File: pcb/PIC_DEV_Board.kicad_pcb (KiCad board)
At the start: 2 copper layers, 25.5 x 47.5 mm, 8 parts, among them J1 Conn_01x08_Pin, J3 Conn_01x15_Pin, J4 Conn_01x02_Pin

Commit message: trace updates
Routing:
- net Net-(J3-Pin_11): track 27.6 -> 26.6 mm
- net Net-(J3-Pin_9): track 21.9 -> 21.3 mm
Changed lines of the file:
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@@
 		(tags "resistor")
 		(property "Reference" "R1"
-			(at 0 -1.65 360)
+			(at 0 -1.65 0)
 			(layer "F.SilkS")
 			(effects
@@
 		)
 		(property "Value" "10K"
-			(at 0 1.65 360)
+			(at 0 1.65 0)
 			(layer "F.Fab")
 			(effects
@@
 		)
 		(fp_text user "${REFERENCE}"
-			(at 0 0 360)
+			(at 0 0 0)
 			(layer "F.Fab")
 			(effects
@@
 	)
 	(segment
-		(start 140.2 113.3)
-		(end 144.6 108.9)
+		(start 137 113.3)
+		(end 142.2 113.3)
 		(width 0.2)
 		(layer "F.Cu")
@@
 	)
 	(segment
-		(start 137 113.3)
-		(end 140.2 113.3)
+		(start 142.2 113.3)
+		(end 144.9 110.6)
 		(width 0.2)
 		(layer "F.Cu")
@@
 	)
 	(segment
-		(start 144.6 108.9)
-		(end 144.6 106.834314)
+		(start 144.9 106.834314)
+		(end 150.924314 100.81)
 		(width 0.2)
 		(layer "F.Cu")
@@
 	)
 	(segment
-		(start 144.6 106.834314)
-		(end 150.624314 100.81)
+		(start 144.9 110.6)
+		(end 144.9 106.834314)
 		(width 0.2)
 		(layer "F.Cu")
@@
 	)
 	(segment
-		(start 150.624314 100.81)
-		(end 152.5 100.81)
-		(width 0.2)
-		(layer "F.Cu")
-		(net 13)
-	)
-	(segment
-		(start 150.65 103.35)
-		(end 152.5 103.35)
+		(start 146.1 117)
+		(end 144.72 118.38)
 		(width 0.2)
 		(layer "F.Cu")
@@
 	)
 	(segment
-		(start 146 118)
-		(end 146 108)
+		(start 151.475001 103.35)
+		(end 146.1 108.725001)
 		(width 0.2)
 		(layer "F.Cu")
@@
 	)
 	(segment
-		(start 137 118.38)
-		(end 145.62 118.38)
+		(start 146.1 108.725001)
+		(end 146.1 117)
 		(width 0.2)
 		(layer "F.Cu")
@@
 	)
 	(segment
-		(start 145.62 118.38)
-		(end 146 118)
+		(start 144.72 118.38)
+		(end 137 118.38)
 		(width 0.2)
 		(layer "F.Cu")
@@
 	)
 	(segment
-		(start 146 108)
-		(end 150.65 103.35)
-		(width 0.2)
-		(layer "F.Cu")
+		(start 152.5 103.35)
+		(end 151.475001 103.35)
+		(width 0.2)
+		(layer "F.Cu")

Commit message: silkscreen
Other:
- board text added: "+"
- board text added: "-"
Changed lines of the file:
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@@
 		(tags "LED")
 		(property "Reference" "D1"
-			(at 0.0625 1.5 180)
+			(at -0.1375 -1.9 180)
 			(layer "F.SilkS")
 			(effects
@@
 		(tags "resistor")
 		(property "Reference" "R2"
-			(at -1.475 -2 0)
+			(at 0.0875 1.9 0)
 			(layer "F.SilkS")
 			(effects
@@
 		(tags "Through hole pin header THT 1x02 2.54mm single row")
 		(property "Reference" "J4"
-			(at 0 -2.33 0)
-			(layer "F.SilkS")
+			(at 2.3 -1.3 0)
+			(layer "F.SilkS")
+			(hide yes)
 			(effects
 				(font
@@
 			(at 0 -2.33 0)
 			(layer "F.SilkS")
+			(hide yes)
 			(effects
 				(font
@@
 		(tags "SOIC SO")
 		(property "Reference" "U1"
-			(at 0.15 7.175 0)
+			(at -0.05 7.685 0)
 			(layer "F.SilkS")
 			(effects
@@
 		(layer "Edge.Cuts")
 	)
+	(gr_text "-\n"
+		(at 139.9 86.6 90)
+		(layer "F.SilkS")
+		(effects
+			(font
+				(size 1.5 1.5)
+				(thickness 0.3)
+				(bold yes)
+			)
+			(justify left bottom)
+		)
+	)
+	(gr_text "+"
+		(at 138.1 91.7 0)
+		(layer "F.SilkS")
+		(effects
+			(font
+				(size 1.5 1.5)
+				(thickness 0.3)
+				(bold yes)
+			)
+			(justify left bottom)
+		)
+	)
 	(segment

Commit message: higher functionality board
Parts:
- removed J3: Conn_01x15_Pin, Connector_PinHeader_2.54mm:PinHeader_1x15_P2.54mm_Vertical
- added C2: 30pF, Capacitor_SMD:C_0805_2012Metric, F.Cu at (136.1, 91.9)
- added C3: 30pF, Capacitor_SMD:C_0805_2012Metric, F.Cu at (136.1, 95.0)
- added C4: 0.1uF, Capacitor_SMD:C_0805_2012Metric, F.Cu at (121.8, 118.3)
- added C5: 10uF, Capacitor_SMD:C_0805_2012Metric, F.Cu at (119.8, 118.3)
- added C6: 0.1uF, Capacitor_SMD:C_0805_2012Metric, F.Cu at (125.2, 93.0)
- added C7: 10uF, Capacitor_SMD:C_0805_2012Metric, F.Cu at (123.2, 93.0)
- added C8: 0.1uF, Capacitor_SMD:C_0805_2012Metric, F.Cu at (163.7, 109.2)
- added C9: 10uF, Capacitor_SMD:C_0805_2012Metric, F.Cu at (161.7, 109.2)
- added D2: LED, LED_SMD:LED_0805_2012Metric, F.Cu at (203.0, 109.3)
- added D3: LED, LED_SMD:LED_0805_2012Metric, F.Cu at (203.0, 111.3)
- added D4: LED, LED_SMD:LED_0805_2012Metric, F.Cu at (203.0, 113.2)
- added D5: LED, LED_SMD:LED_0805_2012Metric, F.Cu at (203.0, 115.2)
- added D6: LED, LED_SMD:LED_0805_2012Metric, F.Cu at (203.0, 117.1)
- added D7: LED, LED_SMD:LED_0805_2012Metric, F.Cu at (203.0, 119.1)
- added D8: LED, LED_SMD:LED_0805_2012Metric, F.Cu at (203.0, 121.0)
- added D9: LED, LED_SMD:LED_0805_2012Metric, F.Cu at (203.0, 123.0)
- added J2: USB_A, Connector_USB:USB_A_Receptacle_GCT_USB1046, F.Cu at (175.0, 83.0)
- added R10: 10K, Resistor_SMD:R_0805_2012Metric, F.Cu at (143.8, 122.4)
- added R11: 560, Resistor_SMD:R_0805_2012Metric, F.Cu at (199.3, 109.3)
- added R12: 560, Resistor_SMD:R_0805_2012Metric, F.Cu at (199.3, 111.3)
- added R13: 560, Resistor_SMD:R_0805_2012Metric, F.Cu at (199.3, 113.2)
- added R14: 560, Resistor_SMD:R_0805_2012Metric, F.Cu at (199.3, 115.2)
- added R15: 560, Resistor_SMD:R_0805_2012Metric, F.Cu at (199.3, 117.2)
- added R16: 560, Resistor_SMD:R_0805_2012Metric, F.Cu at (199.3, 119.1)
- added R17: 560, Resistor_SMD:R_0805_2012Metric, F.Cu at (199.3, 121.0)
- added R18: 560, Resistor_SMD:R_0805_2012Metric, F.Cu at (199.3, 123.0)
- added R3: 0, Resistor_SMD:R_0805_2012Metric, F.Cu at (169.6, 126.4)
- added R4: 10K, Resistor_SMD:R_0805_2012Metric, F.Cu at (169.6, 124.4)
- added R5: 10K, Resistor_SMD:R_0805_2012Metric, F.Cu at (138.8, 118.4)
- added R6: 10K, Resistor_SMD:R_0805_2012Metric, F.Cu at (138.8, 120.4)
- added R7: 10K, Resistor_SMD:R_0805_2012Metric, F.Cu at (138.8, 122.4)
- added R8: 10K, Resistor_SMD:R_0805_2012Metric, F.Cu at (143.8, 118.4)
- added R9: 10K, Resistor_SMD:R_0805_2012Metric, F.Cu at (143.8, 120.4)
- added U2: ~, Package_SO:SOIC-8_3.9x4.9mm_P1.27mm, F.Cu at (161.0, 114.0)
- added U3: MCP3002, Package_SO:SOIC-8_3.9x4.9mm_P1.27mm, F.Cu at (122.5, 98.0)
- added U4: MCP4801, Package_SO:SOIC-8_3.9x4.9mm_P1.27mm, F.Cu at (122.5, 123.1)
- added U5: FT230XS, Package_SO:SSOP-16_3.9x4.9mm_P0.635mm, F.Cu at (171.0, 102.0)
- added U6: 74HC595, Package_SO:SOIC-16_3.9x9.9mm_P1.27mm, F.Cu at (186.8, 115.6)
- moved J1 23.8 mm to (137.1, 80.6), turned to 90 degrees
- moved J4 15.5 mm to (122.5, 81.0), turned to 90 degrees
- moved D1 15.4 mm to (132.0, 81.0), turned to 90 degrees
- moved R2 14.5 mm to (129.0, 81.0), turned to 90 degrees
- moved R1 13.8 mm to (136.9, 87.0), turned to -90 degrees
- moved U1 2.69 mm to (145.7, 101.1)
- moved C1 2.44 mm to (141.7, 93.1)
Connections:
- net Net-(J1-Pin_1) renamed /Vpp/RA3/MCLR
- net Net-(J1-Pin_2) renamed +3V3
- U1 pad 10: Net-(J3-Pin_8) -> /SDI
- U1 pad 12: Net-(J3-Pin_14) -> unconnected-(U1-RB5-Pad12)
- U1 pad 5: Net-(J3-Pin_3) -> unconnected-(U1-RC5-Pad5)
- U1 pad 6: Net-(J3-Pin_4) -> /~{DAC_CS}
- U1 pad 7: Net-(J3-Pin_5) -> /~{ADC_CS}
- U1 pad 8: Net-(J3-Pin_6) -> /SCK
- U1 pad 9: Net-(J3-Pin_7) -> /SDO
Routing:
- net /SDI: track 0.00 -> 60.9 mm
- net Earth: track 16.8 -> 73.0 mm, vias 4 -> 30
- net /~{DAC_CS}: track 0.00 -> 50.0 mm
- net /SCK: track 0.00 -> 47.7 mm
- net Net-(J3-Pin_14): track 31.6 -> 0.00 mm
- net Net-(U6-QD): track 0.00 -> 24.3 mm
- net /~{ADC_CS}: track 0.00 -> 23.9 mm
- net Net-(U2-A2): track 0.00 -> 22.0 mm
- net Net-(U6-QE): track 0.00 -> 21.8 mm
- net Net-(U2-A1): track 0.00 -> 21.7 mm
- net Net-(U2-A0): track 0.00 -> 21.4 mm
- net Net-(U6-QF): track 0.00 -> 20.5 mm
- net Net-(U1-RC2): track 28.6 -> 48.3 mm
- net /SDO: track 0.00 -> 18.9 mm
- net Net-(U6-QG): track 0.00 -> 18.8 mm
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- added copper zone on In2.Cu, net +3V3
- added copper zone on In1.Cu, net Earth
- removed copper zone on B.Cu, net Earth
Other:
- board size 25.5 x 47.5 mm -> 97 x 55 mm
- copper layers 2 -> 4
- board text added: "3P3"
- board text added: "ADC"
- board text added: "DAC"
- board text added: "EEPROM"
- board text added: "FTDI"
- board text added: "GND"
- board text added: "I2C EEPROM ADDRESS"
- board text removed: "+"
- board text removed: "-"

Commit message: size reduction
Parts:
- removed C2, C3: 30pF, Capacitor_SMD:C_0805_2012Metric
- removed D3, D4, D5, D6, D7, D8, D9: LED, LED_SMD:LED_0805_2012Metric
- removed J2: USB_A, Connector_USB:USB_A_Receptacle_GCT_USB1046
- removed R10, R4, R5, R6, R7, R8, R9: 10K, Resistor_SMD:R_0805_2012Metric
- removed R11, R12, R13, R14, R15, R16, R17, R18: 560, Resistor_SMD:R_0805_2012Metric
- added J3: Conn_01x02_Pin, Connector_PinHeader_2.54mm:PinHeader_1x02_P2.54mm_Vertical, F.Cu at (131.0, 89.7)
- added J5: Conn_01x01_Pin, Connector_PinHeader_2.54mm:PinHeader_1x01_P2.54mm_Vertical, F.Cu at (131.0, 108.8)
- R3: value 0 -> 1K
- U6: value 74HC595 -> ~; footprint Package_SO:SOIC-16_3.9x9.9mm_P1.27mm -> myCustomFootprints:USB-A1HSB6
- moved D2 76.4 mm to (130.8, 84.5), turned to 90 degrees
- moved R3 55.7 mm to (132.8, 84.6), turned to 90 degrees
- moved U6 38.1 mm to (160.3, 88.2), turned to 180 degrees
- moved J1 31.8 mm to (166.5, 92.9), turned to 0 degrees
- moved U5 26.2 mm to (148.1, 89.3), turned to 180 degrees
- moved R1 24.6 mm to (160.0, 95.4)
- moved U4 22.4 mm to (133.5, 103.5), turned to 180 degrees
- moved C5 19.2 mm to (136.2, 108.3), turned to 90 degrees
- moved C4 15.9 mm to (134.2, 108.3), turned to -90 degrees
- moved C6 12.5 mm to (137.8, 92.5)
- moved C7 12.5 mm to (135.8, 92.5)
- moved U3 11.0 mm to (133.5, 97.2)
- moved U2 9.49 mm to (158.0, 105.0), turned to 180 degrees
- moved R2 8.64 mm to (137.3, 78.7), turned to 0 degrees
- moved C8 8.47 mm to (155.3, 109.8), turned to -90 degrees
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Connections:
- R3 pad 1: Earth -> Net-(U1-RA5)
- R3 pad 2: Net-(U2-WP) -> Net-(D2-A)
- U1 pad 14: Net-(U1-RC2) -> unconnected-(U1-RC2-Pad14)
- U1 pad 15: Net-(U1-RC1) -> unconnected-(U1-RC1-Pad15)
- U1 pad 3: Net-(U1-RA4) -> unconnected-(U1-RA4-Pad3)
- U2 pad 1: Net-(U2-A0) -> Earth
- U2 pad 2: Net-(U2-A1) -> Earth
- U2 pad 3: Net-(U2-A2) -> Earth
- U2 pad 7: Net-(U2-WP) -> Earth
- U3 pad 2: unconnected-(U3-CH0-Pad2) -> Net-(J3-Pin_1)
- U3 pad 3: unconnected-(U3-CH1-Pad3) -> Net-(J3-Pin_2)
- U4 pad 8: unconnected-(U4-Vout-Pad8) -> Net-(J5-Pin_1)
- U5 pad 8: Net-(J2-D+) -> Net-(U5-USBDP)
- U5 pad 9: Net-(J2-D-) -> Net-(U5-USBDM)
- U6 pad 1: Net-(U6-QB) -> unconnected-(U6-VCC-Pad1)
- U6 pad 2: Net-(U6-QC) -> Net-(U5-USBDM)
- U6 pad 3: Net-(U6-QD) -> Net-(U5-USBDP)
- U6 pad 4: Net-(U6-QE) -> Earth
- U6 pad 5: Net-(U6-QF) -> (no net)
- U6 pad 6: Net-(U6-QG) -> (no net)
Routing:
- net /SDI: track 60.9 -> 10.6 mm
- net Net-(U1-RC2): track 48.3 -> 0.00 mm
- net Net-(U1-RC1): track 43.8 -> 0.00 mm
- net /SCK: track 47.7 -> 10.6 mm
- net /~{DAC_CS}: track 50.0 -> 14.5 mm
- net Earth: track 73.0 -> 43.1 mm, vias 30 -> 22
- net Net-(U6-QD): track 24.3 -> 0.00 mm
- net Net-(U2-A2): track 22.0 -> 0.00 mm
- net /Vpp/RA3/MCLR: track 26.4 -> 48.2 mm
- net Net-(U6-QE): track 21.8 -> 0.00 mm
- net Net-(U2-A1): track 21.7 -> 0.00 mm
- net Net-(U1-RA5): track 0.00 -> 21.6 mm
- net Net-(U2-A0): track 21.4 -> 0.00 mm
- net Net-(U6-QF): track 20.5 -> 0.00 mm
- net +3V3: track 50.0 -> 30.8 mm, vias 12 -> 10
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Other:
- board size 97 x 55 mm -> 41.8 x 38.8 mm
- board text removed: "3P3"
- board text removed: "ADC"
- board text removed: "DAC"
- board text removed: "EEPROM"
- board text removed: "FTDI"
- board text removed: "GND"
- board text removed: "I2C EEPROM ADDRESS"

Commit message: layout changes
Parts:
- added C2: 0.1uF, Capacitor_SMD:C_0805_2012Metric, F.Cu at (153.2, 96.7)
- added C3: 10uF, Capacitor_SMD:C_0805_2012Metric, F.Cu at (156.6, 91.5)
- added R4: 10K, Resistor_SMD:R_0805_2012Metric, F.Cu at (160.8, 90.0)
- added R5: 4.7K, Resistor_SMD:R_0805_2012Metric, F.Cu at (160.8, 88.0)
- added TP1: TestPoint, TestPoint:TestPoint_Pad_1.5x1.5mm, F.Cu at (150.0, 110.0)
- added TP2: TestPoint, TestPoint:TestPoint_Pad_1.5x1.5mm, F.Cu at (147.5, 110.0)
- moved R2 49.4 mm to (174.3, 111.5)
- moved D1 49.4 mm to (174.3, 109.5)
- moved J4 49.3 mm to (166.2, 110.8)
- moved J1 29.0 mm to (139.1, 83.5), turned to 90 degrees
- moved R1 21.0 mm to (140.9, 86.8), turned to 0 degrees
- moved U5 12.0 mm to (157.8, 96.5), turned to 90 degrees
- moved U6 10.1 mm to (165.8, 96.8), turned to 90 degrees
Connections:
- U5 pad 10: unconnected-(U5-3V3OUT-Pad10) -> Net-(U5-3V3OUT)
- U5 pad 11: unconnected-(U5-~{RESET}-Pad11) -> Net-(U5-3V3OUT)
- U5 pad 16: unconnected-(U5-CBUS3-Pad16) -> Net-(U5-CBUS3)
- U5 pad 3: unconnected-(U5-VCCIO-Pad3) -> Net-(U5-3V3OUT)
- U6 pad 1: unconnected-(U6-VCC-Pad1) -> Net-(U6-VCC)
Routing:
- net /Vpp/RA3/MCLR: track 48.2 -> 20.5 mm
- net Net-(U5-3V3OUT): track 0.00 -> 13.4 mm
- net Net-(U5-VCC): track 0.00 -> 11.7 mm
- net Net-(U5-USBDM): track 17.1 -> 6.54 mm
- net Earth: track 43.1 -> 53.0 mm, vias 22 -> 23
- net Net-(U5-CBUS3): track 0.00 -> 9.12 mm
- net +3V3: track 30.8 -> 38.7 mm, vias 10 -> 9
- net /SCK: track 10.6 -> 18.3 mm
- net Net-(U1-RA2): track 9.79 -> 17.4 mm
- net Net-(U6-VCC): track 0.00 -> 7.04 mm
- net Net-(U5-USBDP): track 12.0 -> 6.34 mm
- net Net-(U1-RC0): track 13.7 -> 19.2 mm
- net Net-(J1-Pin_4): track 17.7 -> 15.3 mm
- net Net-(J1-Pin_5): track 18.3 -> 16.2 mm
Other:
- board size 41.8 x 38.8 mm -> 51 x 32 mm

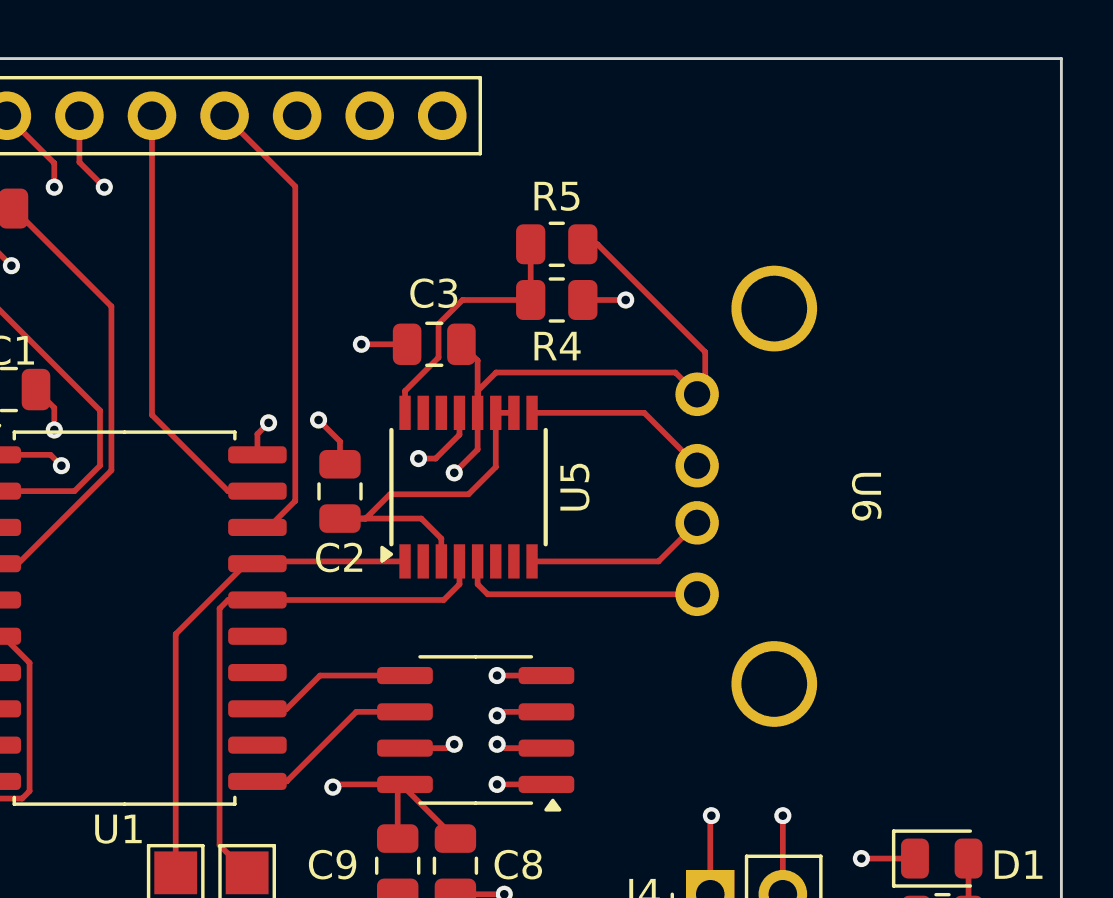
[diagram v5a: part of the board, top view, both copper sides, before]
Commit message: layout/schematic changes
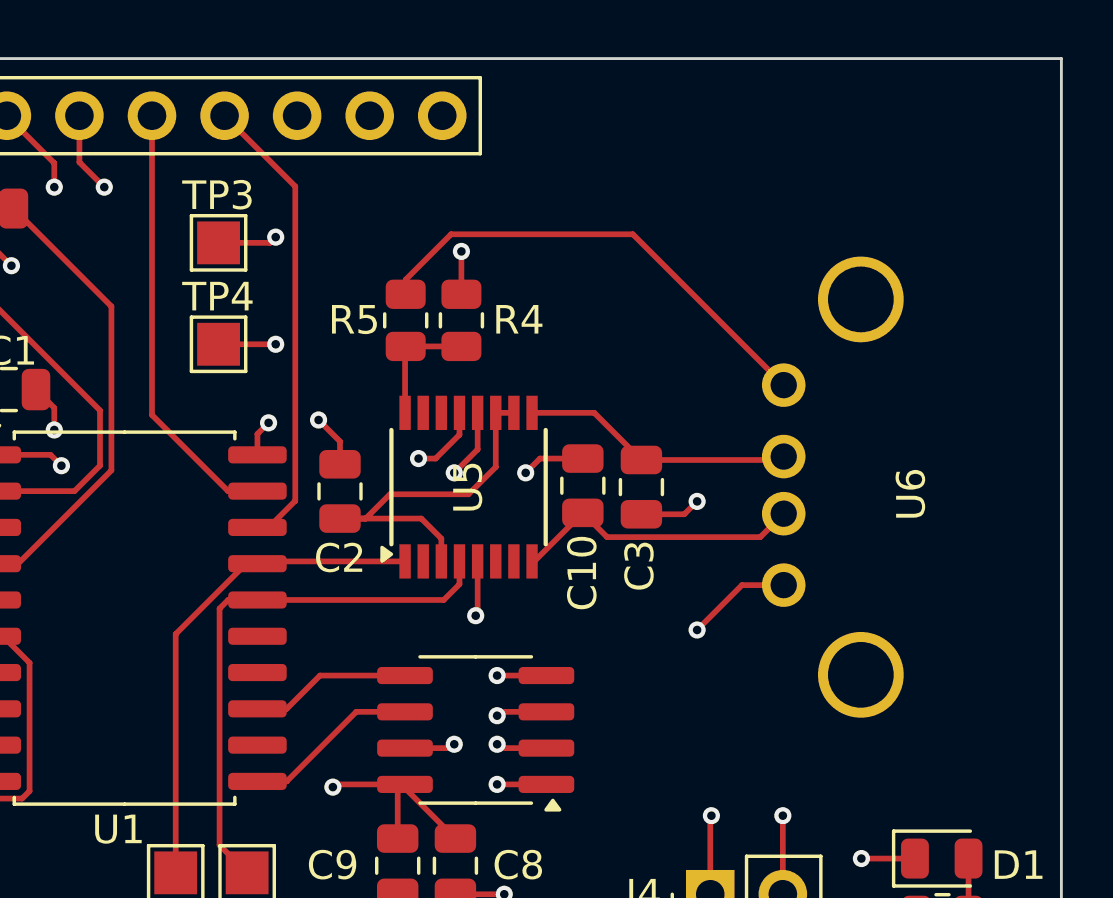
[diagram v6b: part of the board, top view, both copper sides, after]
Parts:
- added C10: 47pF, Capacitor_SMD:C_0805_2012Metric, F.Cu at (161.8, 96.5)
- added TP3: TestPoint, TestPoint:TestPoint_Pad_1.5x1.5mm, F.Cu at (149.0, 88.0)
- added TP4: TestPoint, TestPoint:TestPoint_Pad_1.5x1.5mm, F.Cu at (149.0, 91.5)
- C3: value 10uF -> 47pF
- moved C3 8.81 mm to (163.8, 96.5), turned to -90 degrees
- moved R5 5.92 mm to (155.6, 90.7), turned to 90 degrees
- moved R4 3.41 mm to (157.5, 90.7), turned to -90 degrees
- moved U6 3.05 mm to (168.8, 96.4)
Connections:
- C3 pad 1: Net-(U5-VCC) -> Net-(U5-USBDM)
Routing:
- net Net-(U5-VCC): track 11.7 -> 0.00 mm
- net Net-(U6-VCC): track 7.04 -> 16.6 mm
- net Net-(U5-CBUS3): track 9.12 -> 4.28 mm
- net Net-(U5-USBDP): track 6.34 -> 10.2 mm
- net Net-(U5-USBDM): track 6.54 -> 9.54 mm
- net +3V3: track 38.7 -> 40.8 mm, vias 9 -> 10
- net Earth: track 53.0 -> 54.7 mm, vias 23 -> 27

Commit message: layout/via changes
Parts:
- C6: value 0.1uF -> 10uF
- C7: value 10uF -> 0.1uF
- moved C10 3.76 mm to (165.0, 94.5)
- moved C3 2.29 mm to (165.0, 98.5)
- moved C9 2.06 mm to (155.2, 109.5), turned to -90 degrees
- moved TP2 2.06 mm to (145.5, 110.5)
- moved C8 2.00 mm to (157.2, 109.5)
- moved TP1 0.50 mm to (150.0, 110.5)
- moved R5 0.05 mm to (155.5, 90.7)
- turned C5 to -90 degrees
- turned C7 to 90 degrees
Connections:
- net Net-(U5-CBUS3) renamed /VBUS_SENSE
- C5 pad 1: Earth -> +3V3
- C5 pad 2: +3V3 -> Earth
- C7 pad 1: Earth -> +3V3
- C7 pad 2: +3V3 -> Earth
- C9 pad 1: Earth -> +3V3
- C9 pad 2: +3V3 -> Earth
- U6 pad 1: Net-(U6-VCC) -> Earth
- U6 pad 2: Net-(U5-USBDM) -> Net-(U5-USBDP)
- U6 pad 3: Net-(U5-USBDP) -> Net-(U5-USBDM)
- U6 pad 4: Earth -> Net-(U6-VCC)
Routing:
- net /SDI: track 10.6 -> 28.0 mm, vias 0 -> 2
- net Net-(U6-VCC): track 16.6 -> 23.0 mm, vias 0 -> 2
- net /SCK: track 18.3 -> 24.1 mm, vias 0 -> 2
- net /~{ADC_CS}: track 15.1 -> 19.0 mm, vias 0 -> 2
- net Earth: track 54.7 -> 58.4 mm
- net /~{DAC_CS}: track 14.5 -> 17.1 mm, vias 0 -> 2
- net Net-(U5-3V3OUT): track 13.4 -> 11.3 mm
- net Net-(U1-RA2): track 17.4 -> 18.8 mm
- net Net-(U5-USBDM): track 9.54 -> 10.3 mm
- net Net-(U5-USBDP): track 10.2 -> 11.0 mm, vias 0 -> 2

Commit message: layout/via changes
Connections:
- U1 pad 3: unconnected-(U1-RA4-Pad3) -> Net-(U1-RA4)
- U1 pad 5: unconnected-(U1-RC5-Pad5) -> Net-(U1-RC5)
- U4 pad 5: unconnected-(U4-~{LDAC}-Pad5) -> Net-(U1-RC5)
- U4 pad 6: unconnected-(U4-~{SHDN}-Pad6) -> Net-(U1-RA4)
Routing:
- net Net-(U1-RA4): track 0.00 -> 27.4 mm, vias 0 -> 2
- net Net-(U1-RC5): track 0.00 -> 21.3 mm, vias 0 -> 2
